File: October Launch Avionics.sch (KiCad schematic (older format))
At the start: 1 part

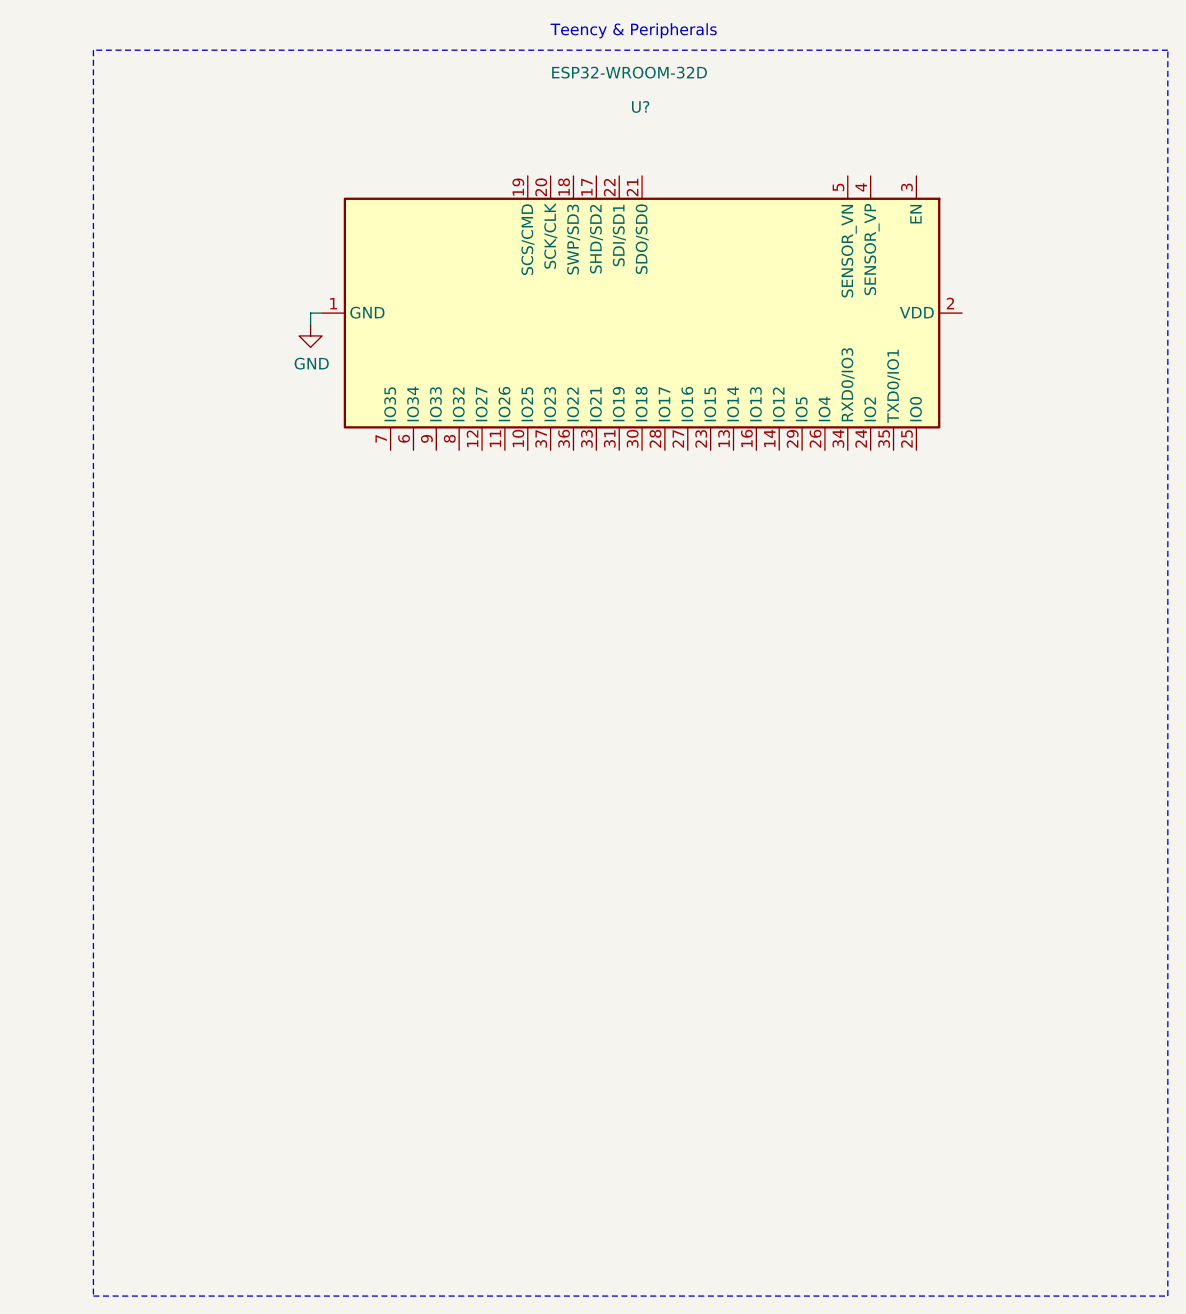
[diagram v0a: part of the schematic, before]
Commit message: Added ICs
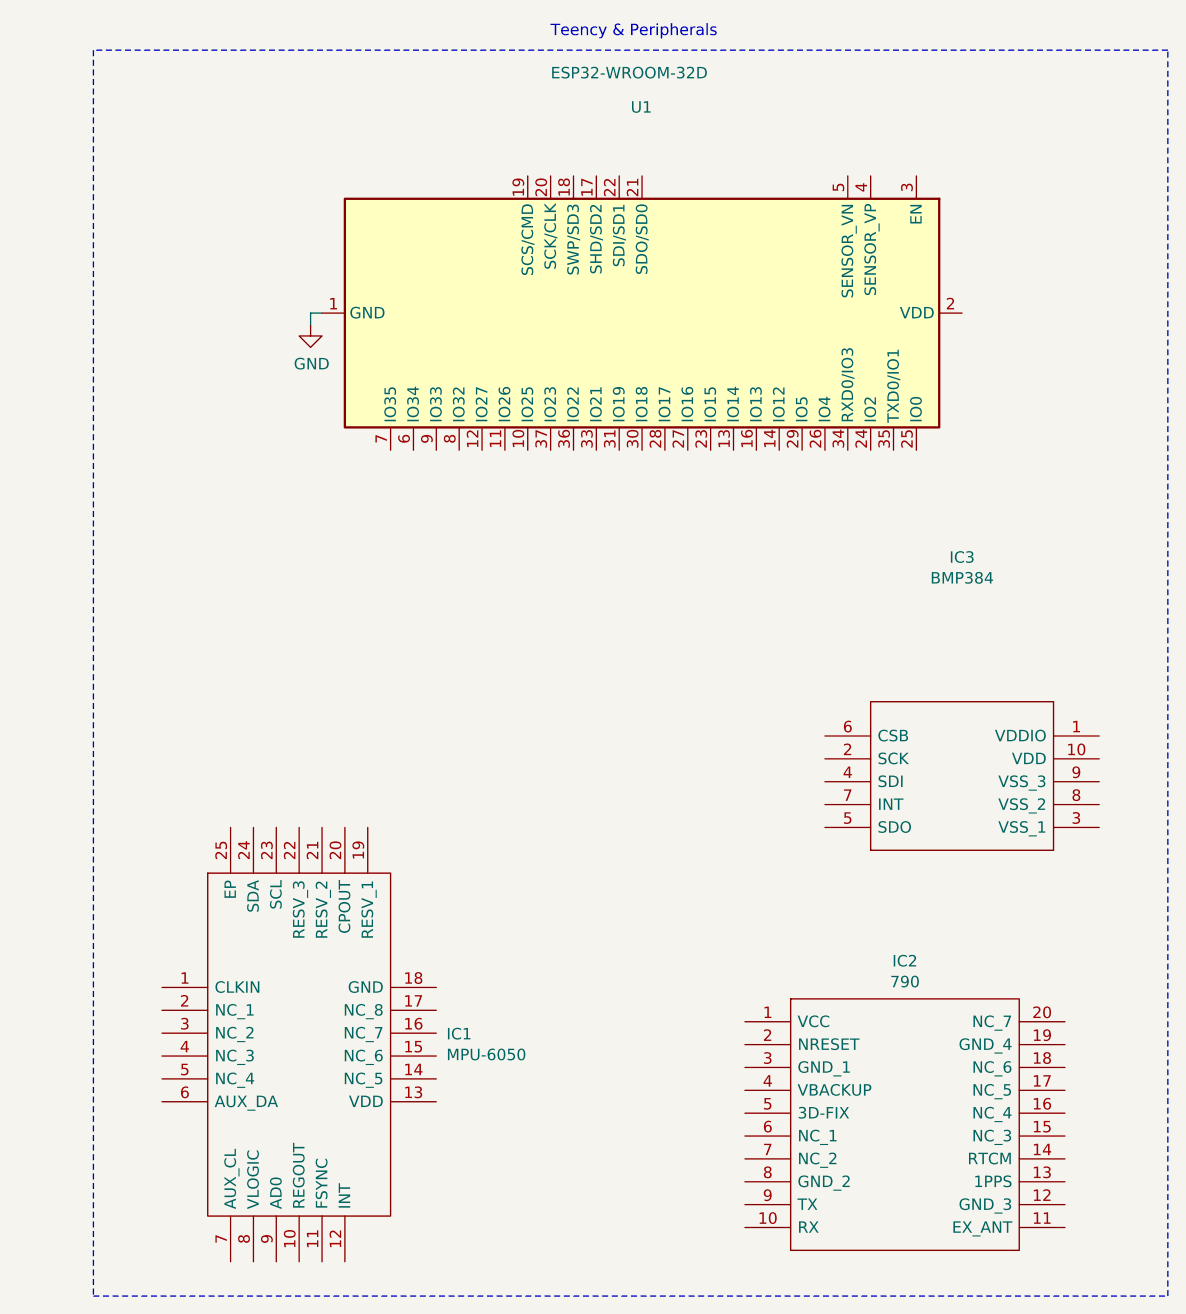
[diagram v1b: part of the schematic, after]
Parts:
- added IC1: MPU-6050, QFN50P400X400X95-25N, symbol SamacSys_Parts:MPU-6050
- added IC2: 790, 790, symbol SamacSys_Parts:790
- added IC3: BMP384, BMP384, symbol SamacSys_Parts:BMP384
- gave numbers to parts that had none: 1
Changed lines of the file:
@@
 Teency & Peripherals
 $Comp
-L RF_Module:ESP32-WROOM-32D U?
+L RF_Module:ESP32-WROOM-32D U1
 U 1 1 60F81389
 P 8400 1950
-F 0 "U?" V 7500 1900 50  0000 L CNN
+F 0 "U1" V 7500 1900 50  0000 L CNN
 F 1 "ESP32-WROOM-32D" V 7350 1550 50  0000 L CNN
 F 2 "RF_Module:ESP32-WROOM-32" H 8400 450 50  0001 C CNN
@@
 $EndComp
 $Comp
-L power:GND #PWR?
+L power:GND #PWR0101
 U 1 1 60F84700
 P 6950 2000
-F 0 "#PWR?" H 6950 1750 50  0001 C CNN
+F 0 "#PWR0101" H 6950 1750 50  0001 C CNN
 F 1 "GND" H 6955 1827 50  0000 C CNN
 F 2 "" H 6950 2000 50  0001 C CNN
@@
 Wire Notes Line
 	850  3000 5000 3000
+$Comp
+L SamacSys_Parts:BMP384 IC3
+U 1 1 61011DE9
+P 9200 3900
+F 0 "IC3" H 9800 4781 50  0000 C CNN
+F 1 "BMP384" H 9800 4690 50  0000 C CNN
+F 2 "BMP384" H 10250 4400 50  0001 L CNN
+F 3 "https://www.mouser.in/datasheet/2/783/bst_bmp384_ds003-1954011.pdf" H 10250 4300 50  0001 L CNN
+F 4 "Board Mount Pressure Sensors Absolute Pressure Sensor" H 10250 4200 50  0001 L CNN "Description"
+F 5 "1" H 10250 4100 50  0001 L CNN "Height"
+F 6 "262-BMP384" H 10250 4000 50  0001 L CNN "Mouser Part Number"
+F 7 "https://www.mouser.co.uk/ProductDetail/Bosch-Sensortec/BMP384?qs=IS%252B4QmGtzzqB3KCclqIEVQ%3D%3D" H 10250 3900 50  0001 L CNN "Mouser Price/Stock"
+F 8 "Bosch Sensortec" H 10250 3800 50  0001 L CNN "Manufacturer_Name"
+F 9 "BMP384" H 10250 3700 50  0001 L CNN "Manufacturer_Part_Number"
+	1    9200 3900
+	1    0    0    -1
+$EndComp
+$Comp
+L SamacSys_Parts:790 IC2
+U 1 1 61012D5C
+P 8850 5050
+F 0 "IC2" H 9550 5315 50  0000 C CNN
+F 1 "790" H 9550 5224 50  0000 C CNN
+F 2 "790" H 10100 5150 50  0001 L CNN
+F 3 "https://cdn-shop.adafruit.com/datasheets/GlobalTop-FGPMMOPA6H-Datasheet-V0A.pdf" H 10100 5050 50  0001 L CNN
+F 4 "GPS Modules Ultimate GPS Module MTK3339 Chipset" H 10100 4950 50  0001 L CNN "Description"
+F 5 "5.2" H 10100 4850 50  0001 L CNN "Height"
+F 6 "485-790" H 10100 4750 50  0001 L CNN "Mouser Part Number"
+F 7 "https://www.mouser.co.uk/ProductDetail/Adafruit/790?qs=GURawfaeGuAcF24Za4dx%252Bw%3D%3D" H 10100 4650 50  0001 L CNN "Mouser Price/Stock"
+F 8 "Adafruit" H 10100 4550 50  0001 L CNN "Manufacturer_Name"
+F 9 "790" H 10100 4450 50  0001 L CNN "Manufacturer_Part_Number"
+	1    8850 5050
+	1    0    0    -1
+$EndComp
+$Comp
+L SamacSys_Parts:MPU-6050 IC1
+U 1 1 61015A99
+P 6300 4900
+F 0 "IC1" H 7544 4696 50  0000 L CNN
+F 1 "MPU-6050" H 7544 4605 50  0000 L CNN
+F 2 "QFN50P400X400X95-25N" H 7350 5400 50  0001 L CNN
+F 3 "https://datasheet.lcsc.com/szlcsc/TDK-InvenSense-MPU-6050_C24112.pdf" H 7350 5300 50  0001 L CNN
+F 4 "IMUs - Inertial Measurement Units 6-Axis MEMS MotionTracking Device with DMP" H 7350 5200 50  0001 L CNN "Description"
+F 5 "0.95" H 7350 5100 50  0001 L CNN "Height"
+F 6 "410-MPU-6050" H 7350 5000 50  0001 L CNN "Mouser Part Number"
+F 7 "https://www.mouser.co.uk/ProductDetail/TDK-InvenSense/MPU-6050?qs=u4fy%2FsgLU9O14B5JgyQFvg%3D%3D" H 7350 4900 50  0001 L CNN "Mouser Price/Stock"
+F 8 "TDK" H 7350 4800 50  0001 L CNN "Manufacturer_Name"
+F 9 "MPU-6050" H 7350 4700 50  0001 L CNN "Manufacturer_Part_Number"
+	1    6300 4900
+	1    0    0    -1
+$EndComp
 $EndSCHEMATC

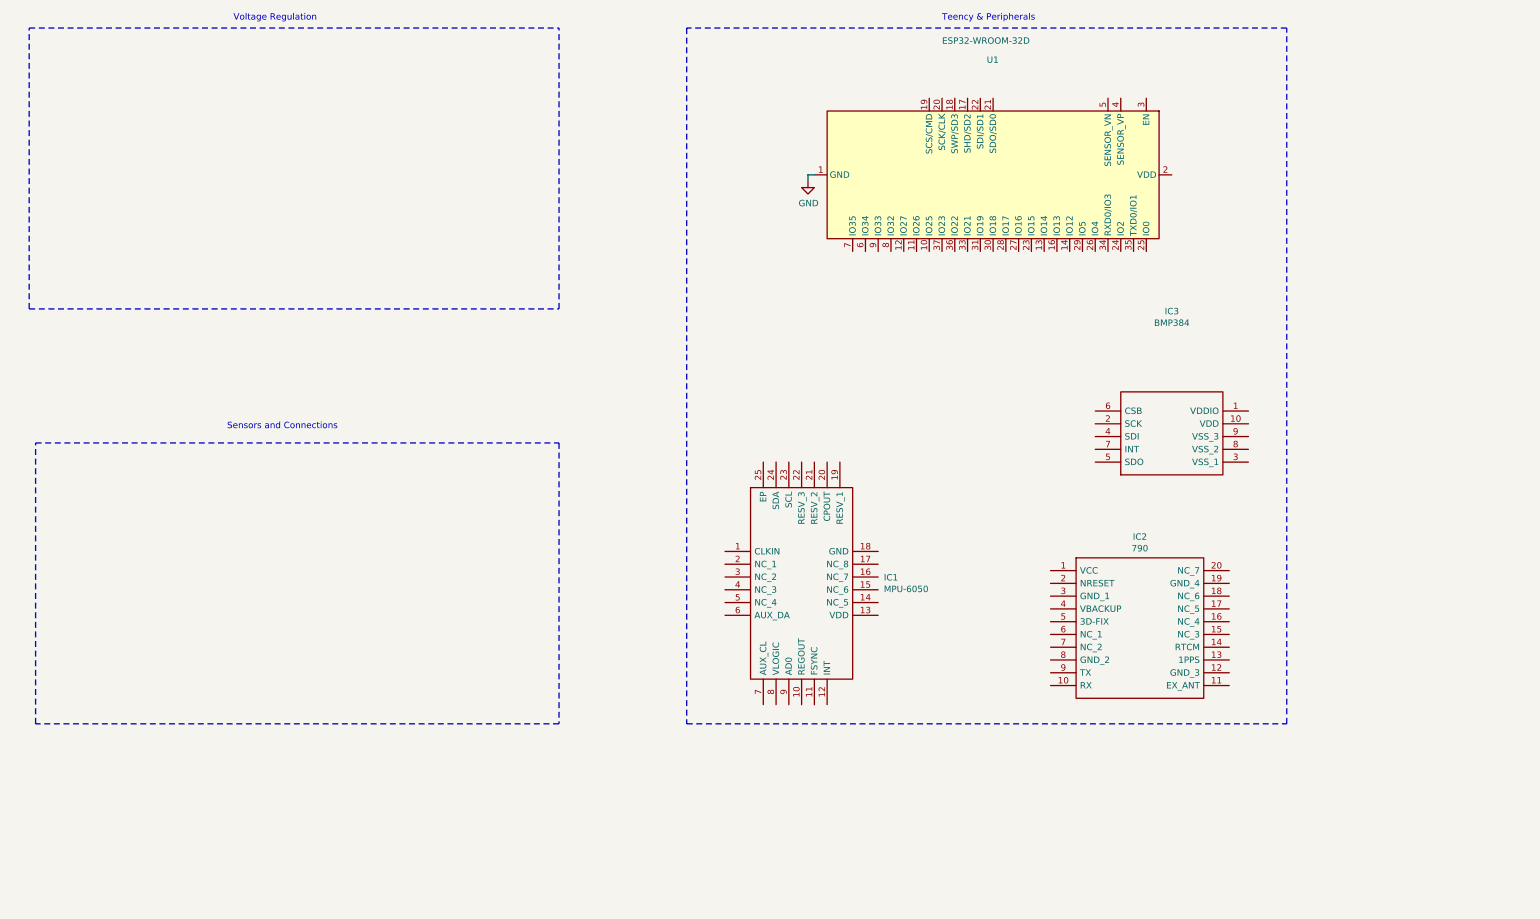
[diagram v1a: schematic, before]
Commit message: Added all sensors + SD Reader & Wired components
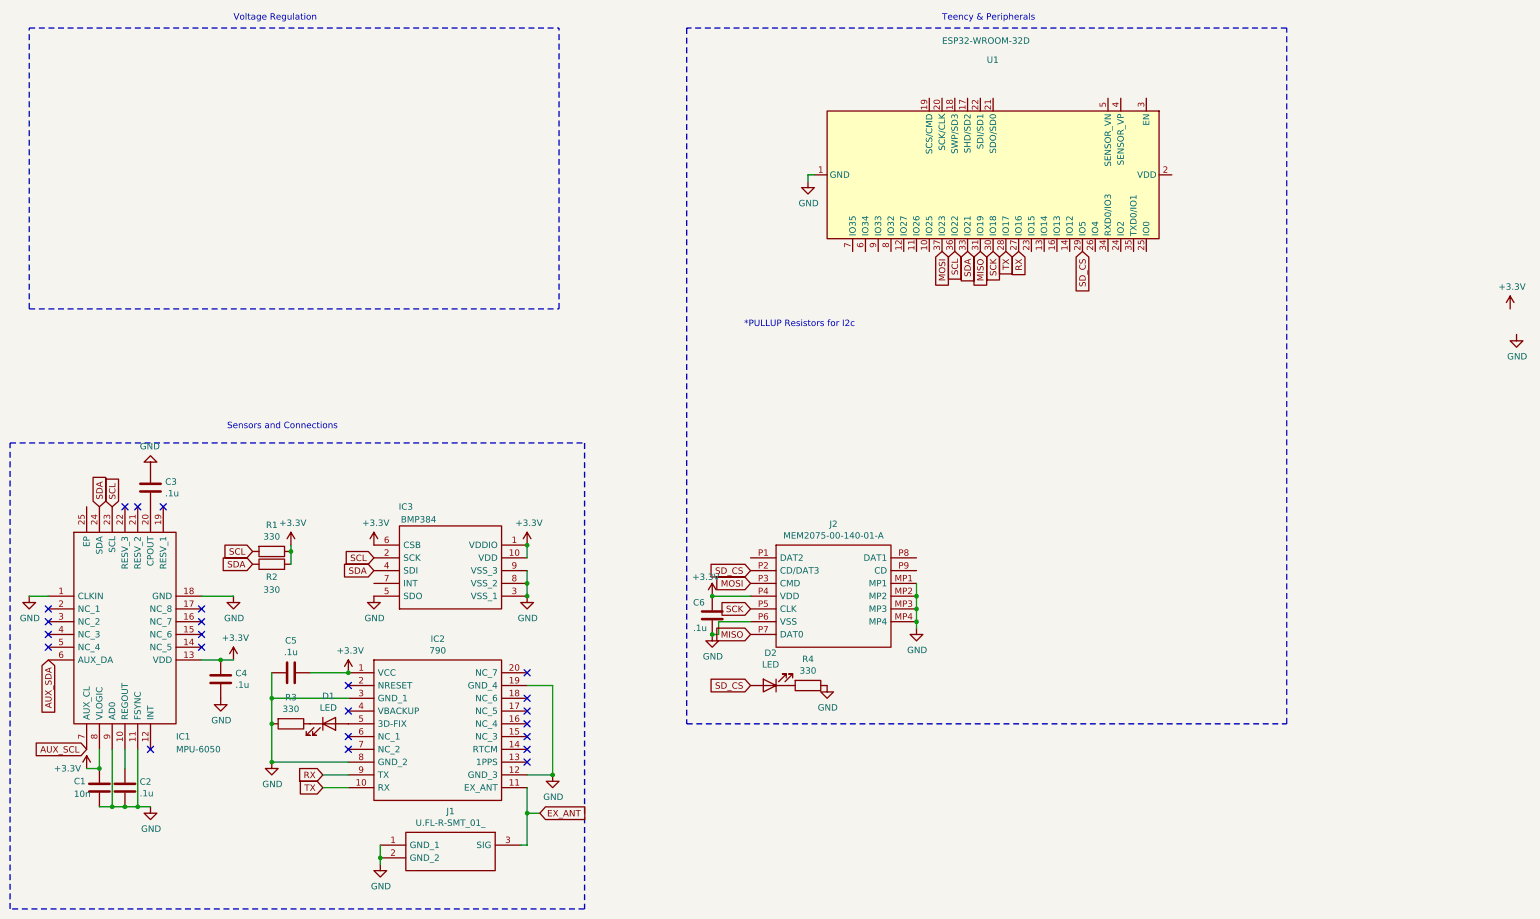
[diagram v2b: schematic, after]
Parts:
- added C1: 10n, symbol Device:C
- added C2, C3, C4, C5, C6: .1u, symbol Device:C
- added D1, D2: LED, symbol Device:LED
- added J1: U.FL-R-SMT_01_, UFLRSMT01, symbol SamacSys_Parts:U.FL-R-SMT_01_
- added J2: MEM2075-00-140-01-A, MEM20750014001A, symbol SamacSys_Parts:MEM2075-00-140-01-A
- added R1, R2, R3, R4: 330, symbol Device:R
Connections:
- net GND: now also IC1.1 (CLKIN), IC1.11 (FSYNC), IC1.18 (GND), IC1.9 (AD0), IC2.12 (GND_3), IC2.19 (GND_4), IC2.3 (GND_1), IC2.8 (GND_2), IC3.3 (VSS_1), IC3.5 (SDO), IC3.8 (VSS_2), IC3.9 (VSS_3), C1.2, C2.2, C3.1, C4.2, C5.2, C6.1, J1.1 (GND_1), J1.2 (GND_2), J2.MP1, J2.MP2, J2.MP3, J2.MP4, J2.P6 (VSS), R3.2, R4.1
- net RX: now reaches U1.27 (IO16)
- net RX: now also IC2.9 (TX)
- net TX: now reaches U1.28 (IO17)
- net TX: now also IC2.10 (RX)
- net SD_CS: now reaches U1.29 (IO5)
- net SD_CS: now also D2.2 (A), J2.P2 (CD/DAT3)
- net SCK: now reaches U1.30 (IO18)
- net SCK: now also J2.P5 (CLK)
- net MISO: now reaches U1.31 (IO19)
- net MISO: now also J2.P7 (DAT0)
- net SDA: now reaches U1.33 (IO21)
- net SDA: now also IC1.24 (SDA), IC3.4 (SDI), R2.1
- net SCL: now reaches U1.36 (IO22)
- net SCL: now also IC1.23 (SCL), IC3.2 (SCK), R1.2
- net MOSI: now reaches U1.37 (IO23)
- net MOSI: now also J2.P3 (CMD)
- net +3V3: now reaches IC3.1 (VDDIO)
- net +3V3: now also IC1.13 (VDD), IC1.8 (VLOGIC), IC2.1 (VCC), IC3.10 (VDD), IC3.6 (CSB), C1.1, C4.1, C5.1, C6.2, J2.P4 (VDD), R1.1, R2.2
- net EX_ANT: now reaches IC2.11 (EX_ANT)
- net EX_ANT: now also J1.3 (SIG)
- net at IC2.5 (3D-FIX): now also D1.2 (A)
- net at IC1.10 (REGOUT): now also C2.1
- net at IC1.20 (CPOUT): now also C3.2
- net AUX_SDA: now reaches IC1.6 (AUX_DA)
- net AUX_SCL: now reaches IC1.7 (AUX_CL)
- new net: D1.1 (K), R3.1
- new net: D2.1 (K), R4.2
- no-connect marks 0 -> 23
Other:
- note added: "*PULLUP Resistors for I2c"
- moved on the sheet: IC1, IC2, IC3
